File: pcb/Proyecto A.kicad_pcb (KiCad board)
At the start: 2 copper layers, 337.3 x 122.6 mm, 187 parts, among them J1 j, K1 1, K10 10, K11 k, K2 2, K3 3, K4 4, K6 6, K7 7, K8 8, K9 9, M1 KEYSW, P1 p, Q1 q, SW1 SW_Push, T1 t, U1 ATmega32U4-AU, U2 u, X1 x, Y1 16MHZ, Y2 y, k5 5

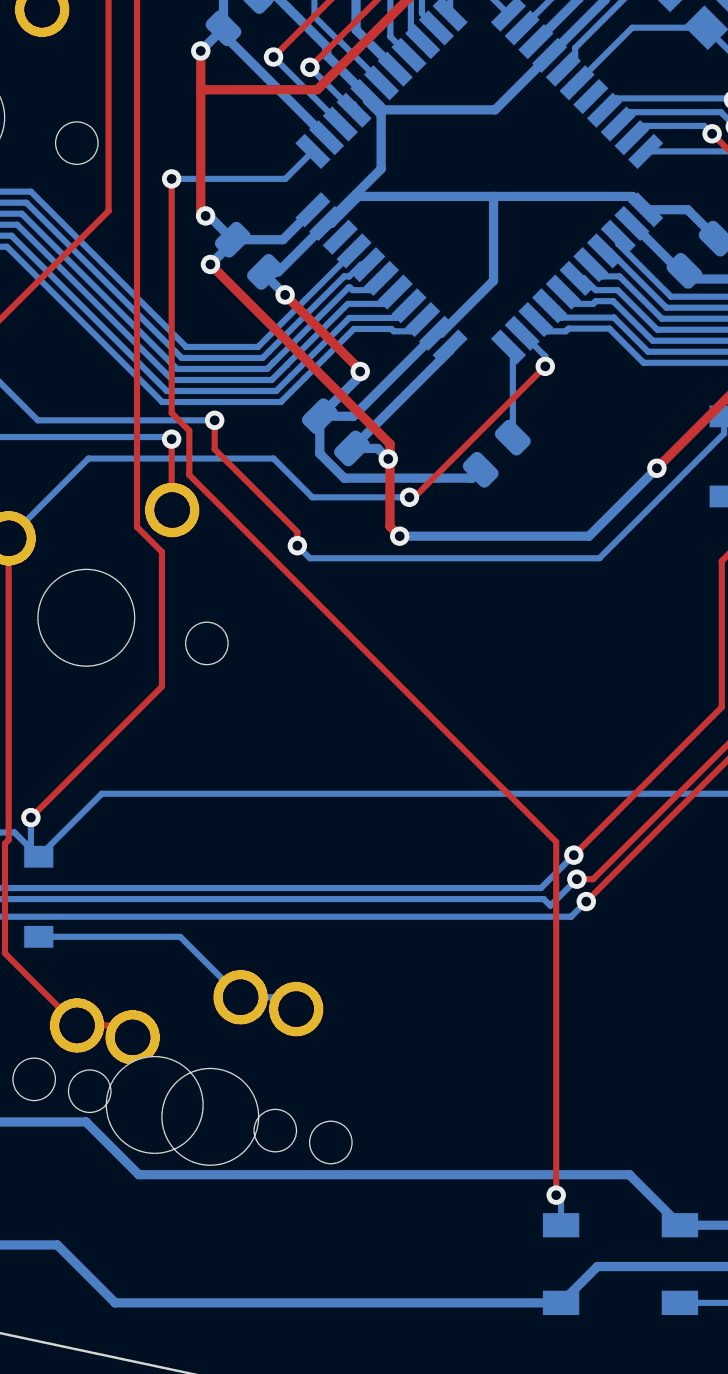
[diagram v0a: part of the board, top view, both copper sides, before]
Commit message: added a 500 ohm resistor bettween mcu underglow pin and 1st ws2812b
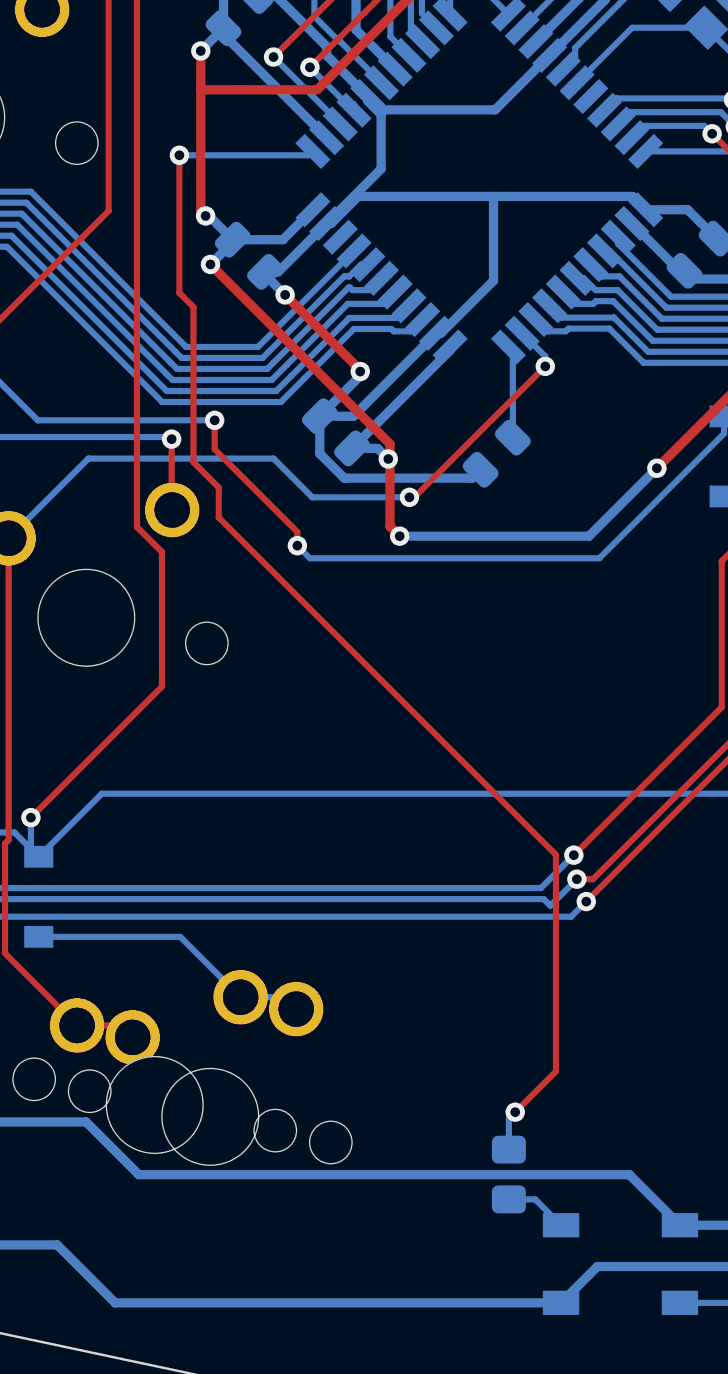
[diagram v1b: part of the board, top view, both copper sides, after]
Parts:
- added R11: 500 ohm, Resistor_SMD:R_0805_2012Metric_Pad1.15x1.40mm_HandSolder, B.Cu at (227.4, 98.7)
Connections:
- D4 pad 4: UNDERGLOW -> Net-(D4-Pad4)
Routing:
- net Net-(D4-Pad4): track 0.00 -> 2.76 mm
- net UNDERGLOW: track 56.1 -> 53.8 mm
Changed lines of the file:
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@@
     (thickness 1.6)
     (drawings 1202)
-    (tracks 1843)
+    (tracks 1849)
     (zones 0)
-    (modules 187)
-    (nets 125)
+    (modules 188)
+    (nets 126)
   )
   (page A4)
@@
       (drillshape 0)
       (scaleselection 1)
-      (outputdirectory "Proyecto A. Prototipo 1. Gerbers/"))
+      (outputdirectory "New folder/"))
   )
   (net 0 "")
@@
   (net 123 "Net-(U1-Pad18)")
   (net 124 "Net-(D_14-Pad2)")
+  (net 125 "Net-(D4-Pad4)")
   (net_class Default "This is the default net class."
     (clearance 0.2)
@@
     (add_net "Net-(D3-Pad1)")
     (add_net "Net-(D4-Pad2)")
+    (add_net "Net-(D4-Pad4)")
     (add_net "Net-(D5-Pad2)")
     (add_net "Net-(D6-Pad2)")
@@
     (add_net VCC)
   )
+  (module Resistor_SMD:R_0805_2012Metric_Pad1.15x1.40mm_HandSolder (layer B.Cu)
+    (at 227.4274 98.697 90)
+    (descr "Resistor SMD 0805 (2012 Metric), square (rectangular) end terminal, IPC_7351 nominal with elongated pad for handsoldering. (Body size source: https://docs.google.com/spreadsheets/d/1BsfQQcO9C6DZCsRaXUlFlo91Tg2WpOkGARC1WS5S8t0/edit?usp=sharing), generated with kicad-footprint-generator")
+    (tags "resistor handsolder")
+    (attr smd)
+    (fp_text reference R11 (at 0 1.65 270) (layer B.SilkS)
+      (effects (font (size 1 1) (thickness 0.15)) (justify mirror))
+    )
+    (fp_text value "500 ohm" (at 0 -1.65 270) (layer B.Fab)
+      (effects (font (size 1 1) (thickness 0.15)) (justify mirror))
+    )
+    (fp_text user %R (at 0 0 270) (layer B.Fab)
+      (effects (font (size 0.5 0.5) (thickness 0.08)) (justify mirror))
+    )
+    (fp_line (start -1 -0.6) (end -1 0.6) (layer B.Fab) (width 0.1))
+    (fp_line (start -1 0.6) (end 1 0.6) (layer B.Fab) (width 0.1))
+    (fp_line (start 1 0.6) (end 1 -0.6) (layer B.Fab) (width 0.1))
+    (fp_line (start 1 -0.6) (end -1 -0.6) (layer B.Fab) (width 0.1))
+    (fp_line (start -0.261252 0.71) (end 0.261252 0.71) (layer B.SilkS) (width 0.12))
+    (fp_line (start -0.261252 -0.71) (end 0.261252 -0.71) (layer B.SilkS) (width 0.12))
+    (fp_line (start -1.85 -0.95) (end -1.85 0.95) (layer B.CrtYd) (width 0.05))
+    (fp_line (start -1.85 0.95) (end 1.85 0.95) (layer B.CrtYd) (width 0.05))
+    (fp_line (start 1.85 0.95) (end 1.85 -0.95) (layer B.CrtYd) (width 0.05))
+    (fp_line (start 1.85 -0.95) (end -1.85 -0.95) (layer B.CrtYd) (width 0.05))
+    (pad 2 smd roundrect (at 1.025 0 90) (size 1.15 1.4) (layers B.Cu B.Paste B.Mask) (roundrect_rratio 0.217391)
+      (net 12 UNDERGLOW))
+    (pad 1 smd roundrect (at -1.025 0 90) (size 1.15 1.4) (layers B.Cu B.Paste B.Mask) (roundrect_rratio 0.217391)
+      (net 125 "Net-(D4-Pad4)"))
+    (model ${KISYS3DMOD}/Resistor_SMD.3dshapes/R_0805_2012Metric.wrl
+      (at (xyz 0 0 0))
+      (scale (xyz 1 1 1))
+      (rotate (xyz 0 0 0))
+    )
+  )
   (module LED_SMD:LED_1206_3216Metric_Pad1.42x1.75mm_HandSolder (layer F.Cu)
     (at 66.2399 84.312)
@@
       (effects (font (size 1 1) (thickness 0.15)))
     )
-    (fp_text user %R (at 0 0) (layer F.Fab)
-      (effects (font (size 0.8 0.8) (thickness 0.12)))
-    )
     (fp_line (start 1.6 -0.8) (end -1.2 -0.8) (layer F.Fab) (width 0.1))
     (fp_line (start -1.2 -0.8) (end -1.6 -0.4) (layer F.Fab) (width 0.1))
@@
     (fp_line (start 2.45 -1.12) (end 2.45 1.12) (layer F.CrtYd) (width 0.05))
     (fp_line (start 2.45 1.12) (end -2.45 1.12) (layer F.CrtYd) (width 0.05))
+    (fp_text user %R (at 0 0) (layer F.Fab)
+      (effects (font (size 0.8 0.8) (thickness 0.12)))
+    )
     (pad 2 smd roundrect (at 1.4875 0) (size 1.425 1.75) (layers F.Cu F.Paste F.Mask) (roundrect_rratio 0.175439)
       (net 9 num))
@@
       (effects (font (size 1 1) (thickness 0.15)))
     )
-    (fp_text user %R (at 0 0) (layer F.Fab)
-      (effects (font (size 0.8 0.8) (thickness 0.12)))
-    )
     (fp_line (start 1.6 -0.8) (end -1.2 -0.8) (layer F.Fab) (width 0.1))
     (fp_line (start -1.2 -0.8) (end -1.6 -0.4) (layer F.Fab) (width 0.1))
@@
     (fp_line (start 2.45 -1.12) (end 2.45 1.12) (layer F.CrtYd) (width 0.05))
     (fp_line (start 2.45 1.12) (end -2.45 1.12) (layer F.CrtYd) (width 0.05))
+    (fp_text user %R (at 0 0) (layer F.Fab)
+      (effects (font (size 0.8 0.8) (thickness 0.12)))
+    )
     (pad 2 smd roundrect (at 1.4875 0) (size 1.425 1.75) (layers F.Cu F.Paste F.Mask) (roundrect_rratio 0.175439)
       (net 122 scrol))
@@
       (effects (font (size 1 1) (thickness 0.15)))
     )
-    (fp_text user %R (at 0 0) (layer F.Fab)
-      (effects (font (size 0.8 0.8) (thickness 0.12)))
-    )
     (fp_line (start 1.6 -0.8) (end -1.2 -0.8) (layer F.Fab) (width 0.1))
     (fp_line (start -1.2 -0.8) (end -1.6 -0.4) (layer F.Fab) (width 0.1))
@@
     (fp_line (start 2.45 -1.12) (end 2.45 1.12) (layer F.CrtYd) (width 0.05))
     (fp_line (start 2.45 1.12) (end -2.45 1.12) (layer F.CrtYd) (width 0.05))
+    (fp_text user %R (at 0 0) (layer F.Fab)
+      (effects (font (size 0.8 0.8) (thickness 0.12)))
+    )
     (pad 2 smd roundrect (at 1.4875 0) (size 1.425 1.75) (layers F.Cu F.Paste F.Mask) (roundrect_rratio 0.175439)
       (net 6 caps))
@@
       (net 11 "Net-(D4-Pad2)"))
     (pad 4 smd rect (at 2.45 1.6 180) (size 1.5 1) (layers B.Cu B.Paste B.Mask)
-      (net 12 UNDERGLOW))
+      (net 125 "Net-(D4-Pad4)"))
     (pad 3 smd rect (at 2.45 -1.6 180) (size 1.5 1) (layers B.Cu B.Paste B.Mask)
       (net 1 GND))
@@
   (segment (start 245.6694 103.987) (end 234.4774 103.987) (width 0.254) (layer B.Cu) (net 11))
   (segment (start 253.0094 96.647) (end 245.6694 103.987) (width 0.254) (layer B.Cu) (net 11))
-  (segment (start 229.5774 100.787) (end 229.5774 99.74784) (width 0.254) (layer B.Cu) (net 12))
-  (via (at 229.37724 99.54768) (size 0.8) (drill 0.4) (layers F.Cu B.Cu) (net 12))
-  (segment (start 229.5774 99.74784) (end 229.37724 99.54768) (width 0.254) (layer B.Cu) (net 12))
-  (via (at 213.52764 57.66054) (size 0.8) (drill 0.4) (layers F.Cu B.Cu) (net 12))
-  (segment (start 229.37724 84.986698) (end 214.254401 69.863859) (width 0.254) (layer F.Cu) (net 12))
-  (segment (start 214.254401 69.863859) (end 214.254401 68.038039) (width 0.254) (layer F.Cu) (net 12))
-  (segment (start 214.254401 68.038039) (end 213.52764 67.311278) (width 0.254) (layer F.Cu) (net 12))
-  (segment (start 229.37724 99.54768) (end 229.37724 84.986698) (width 0.254) (layer F.Cu) (net 12))
-  (segment (start 213.52764 67.311278) (end 213.52764 57.66054) (width 0.254) (layer F.Cu) (net 12))
-  (segment (start 218.215882 57.66054) (end 219.348824 56.527598) (width 0.254) (layer B.Cu) (net 12))
-  (segment (start 213.52764 57.66054) (end 218.215882 57.66054) (width 0.254) (layer B.Cu) (net 12))
+  (segment (start 229.3674 85.517) (end 215.4674 71.617) (width 0.254) (layer F.Cu) (net 12))
+  (segment (start 215.4674 71.617) (end 215.4674 70.377) (width 0.254) (layer F.Cu) (net 12))
+  (segment (start 215.4674 70.377) (end 214.4274 69.337) (width 0.254) (layer F.Cu) (net 12))
+  (segment (start 214.4274 69.337) (end 214.4274 62.947) (width 0.254) (layer F.Cu) (net 12))
+  (via (at 213.8474 56.687) (size 0.8) (drill 0.4) (layers F.Cu B.Cu) (net 12))
+  (segment (start 214.4274 62.947) (end 213.8474 62.367) (width 0.254) (layer F.Cu) (net 12))
+  (segment (start 213.8474 62.367) (end 213.8474 56.687) (width 0.254) (layer F.Cu) (net 12))
+  (segment (start 219.189422 56.687) (end 219.348824 56.527598) (width 0.254) (layer B.Cu) (net 12))
+  (segment (start 213.8474 56.687) (end 219.189422 56.687) (width 0.254) (layer B.Cu) (net 12))
+  (via (at 227.6874 96.127) (size 0.8) (drill 0.4) (layers F.Cu B.Cu) (net 12))
+  (segment (start 227.4274 97.672) (end 227.4274 96.387) (width 0.254) (layer B.Cu) (net 12))
+  (segment (start 227.4274 96.387) (end 227.6874 96.127) (width 0.254) (layer B.Cu) (net 12))
+  (segment (start 229.3674 94.447) (end 229.3674 85.517) (width 0.254) (layer F.Cu) (net 12))
+  (segment (start 227.6874 96.127) (end 229.3674 94.447) (width 0.254) (layer F.Cu) (net 12))
   (segment (start 155.515067 9.359999) (end 147.604401 9.359999) (width 0.254) (layer B.Cu) (net 13))
   (segment (start 147.604401 9.359999) (end 146.7774 10.187) (width 0.254) (layer B.Cu) (net 13))
@@
   (segment (start 366.047933 0.11) (end 370.378966 -4.221033) (width 0.254) (layer B.Cu) (net 124))
   (segment (start 362.02 0.11) (end 366.047933 0.11) (width 0.254) (layer B.Cu) (net 124))
+  (segment (start 229.4574 100.667) (end 229.5774 100.787) (width 0.254) (layer B.Cu) (net 125))
+  (segment (start 228.5124 99.722) (end 229.5774 100.787) (width 0.254) (layer B.Cu) (net 125))
+  (segment (start 227.4274 99.722) (end 228.5124 99.722) (width 0.254) (layer B.Cu) (net 125))
   (zone (net 1) (net_name GND) (layer B.Cu) (hatch edge 0.508)
     (connect_pads (clearance 0.508))

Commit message: Proto 1.1
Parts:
- added G***: LOGO, Logo:Proyecto A 300, F.Cu at (340.1, 82.2)
- C1, C10, C11, C12, C13, C14, C15, C16, C17, C18, C19, C2, C20, C21, C3, C4, C5, C6, C7, C9: footprint Capacitor_SMD:C_0805_2012Metric -> Capacitor_SMD:C_0805_2012Metric_Pad1.15x1.40mm_HandSolder
- USB1: footprint Type-C:HRO-TYPE-C-31-M-12-jlc -> Type-C:HRO-TYPE-C-31-M-12-HandSoldering
- Y1: footprint Crystal:Crystal_SMD_3225-4Pin_3.2x2.5mm -> Crystal:Crystal_SMD_3225-4Pin_3.2x2.5mm_HandSoldering
- moved C4 0.78 mm to (236.0, 60.4)
- moved C6 0.11 mm to (218.7, 48.4)
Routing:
- net GND: track 1043.3 -> 1058.7 mm, vias 38 -> 40
- net +5V: track 1008.1 -> 1002.3 mm, vias 28 -> 30
- net Net-(R2-Pad2): track 7.03 -> 10.6 mm
- net Net-(C3-Pad1): track 10.8 -> 12.9 mm
- net VCC: track 15.8 -> 16.9 mm
- net Net-(R8-Pad2): track 5.07 -> 6.20 mm
- net Net-(R1-Pad2): track 7.87 -> 6.86 mm
- net num: track 234.9 -> 234.3 mm
- net Net-(R9-Pad2): track 5.08 -> 4.58 mm

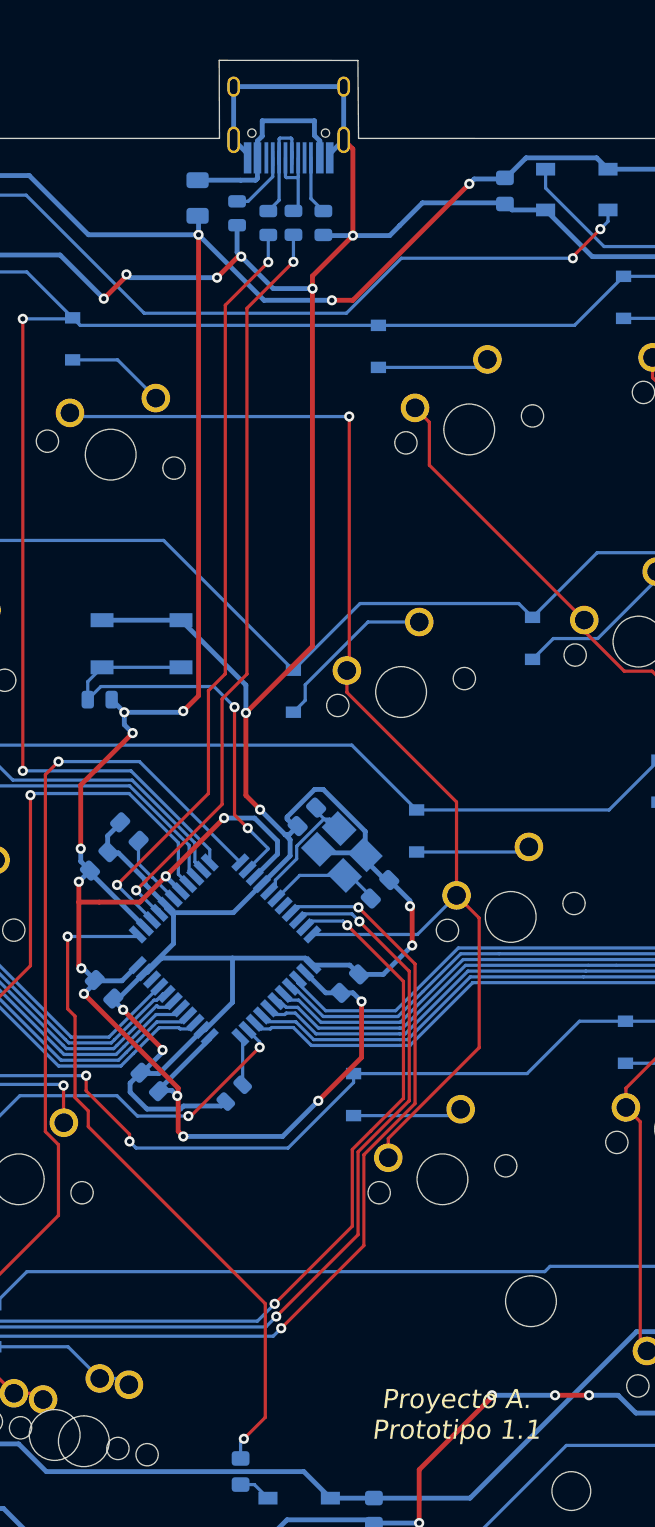
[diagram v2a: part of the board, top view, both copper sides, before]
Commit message: proto 1.2
Moved usb to top side of the pcb
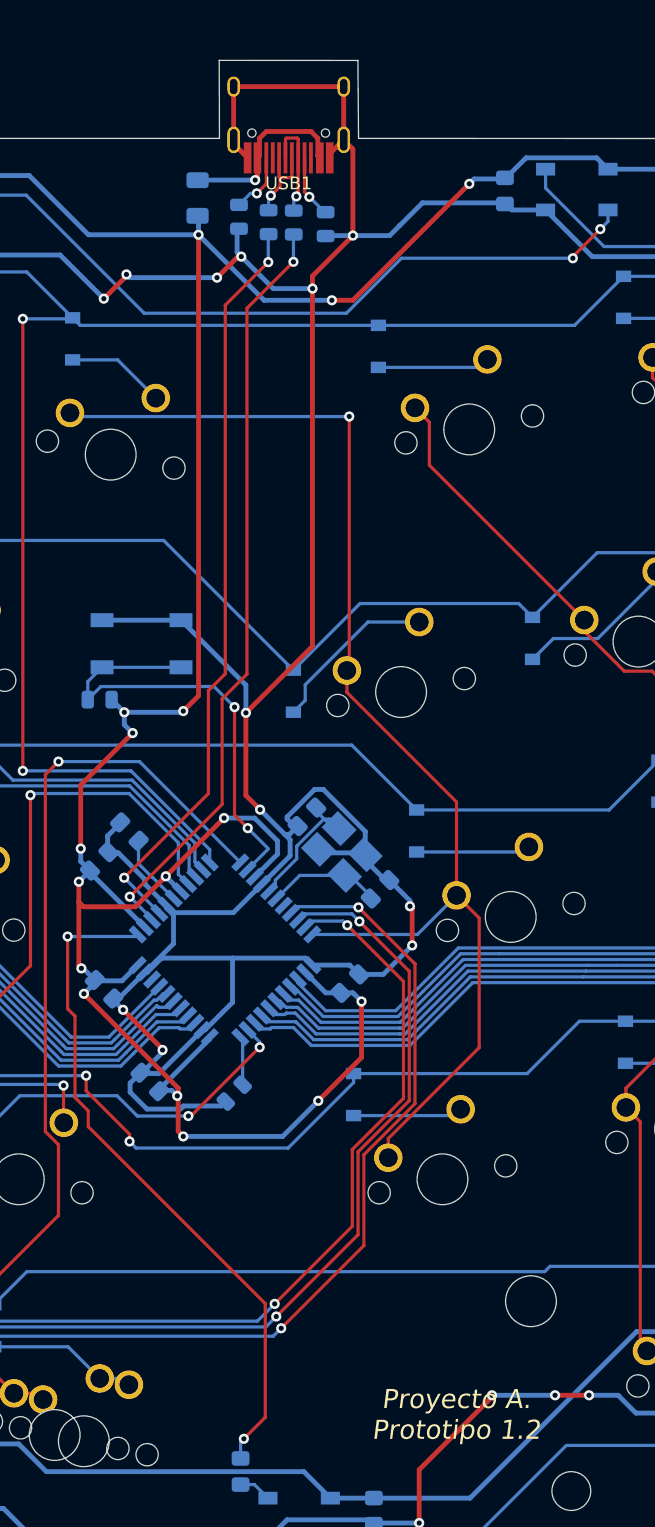
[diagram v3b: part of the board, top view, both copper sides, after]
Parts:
- USB1: moved to F.Cu
- moved R8 7.00 mm to (234.1, 0.75)
- moved R9 6.64 mm to (227.3, 0.17)
- moved R2 2.00 mm to (231.6, 0.62)
- moved R1 1.95 mm to (229.6, 0.60)
- turned USB1 to 180 degrees
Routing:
- net Net-(R2-Pad2): track 10.6 -> 8.30 mm, vias 0 -> 1
- net VCC: track 16.9 -> 14.9 mm, vias 0 -> 1
- net Net-(R8-Pad2): track 6.20 -> 4.99 mm, vias 0 -> 1
- net GND: track 1058.7 -> 1059.5 mm
- net Net-(R9-Pad2): track 4.58 -> 4.87 mm, vias 0 -> 1
- net Net-(R1-Pad2): track 6.86 -> 6.95 mm, vias 0 -> 1
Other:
- board text added: "Proyecto A. Prototipo 1.2"
- board text removed: "Proyecto A. Prototipo 1.1"
